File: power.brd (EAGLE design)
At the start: 186 x 186 mm, 126 parts, among them CN2 2X10 HEADER, Q1 IXTK180N15P, Q2 IXTK180N15P, Q3 2N7002, Q4 SPD15P10PL, Q5 2N7002, U1 LT1630, U10 LM2936, U11 LM317, U2 LT1630, U3 DCDC 15V, U4 DAC80501, U5 DAC80501, U6 ADS1120, U7 LM2662, U8 LM7805, U9 TPS3700

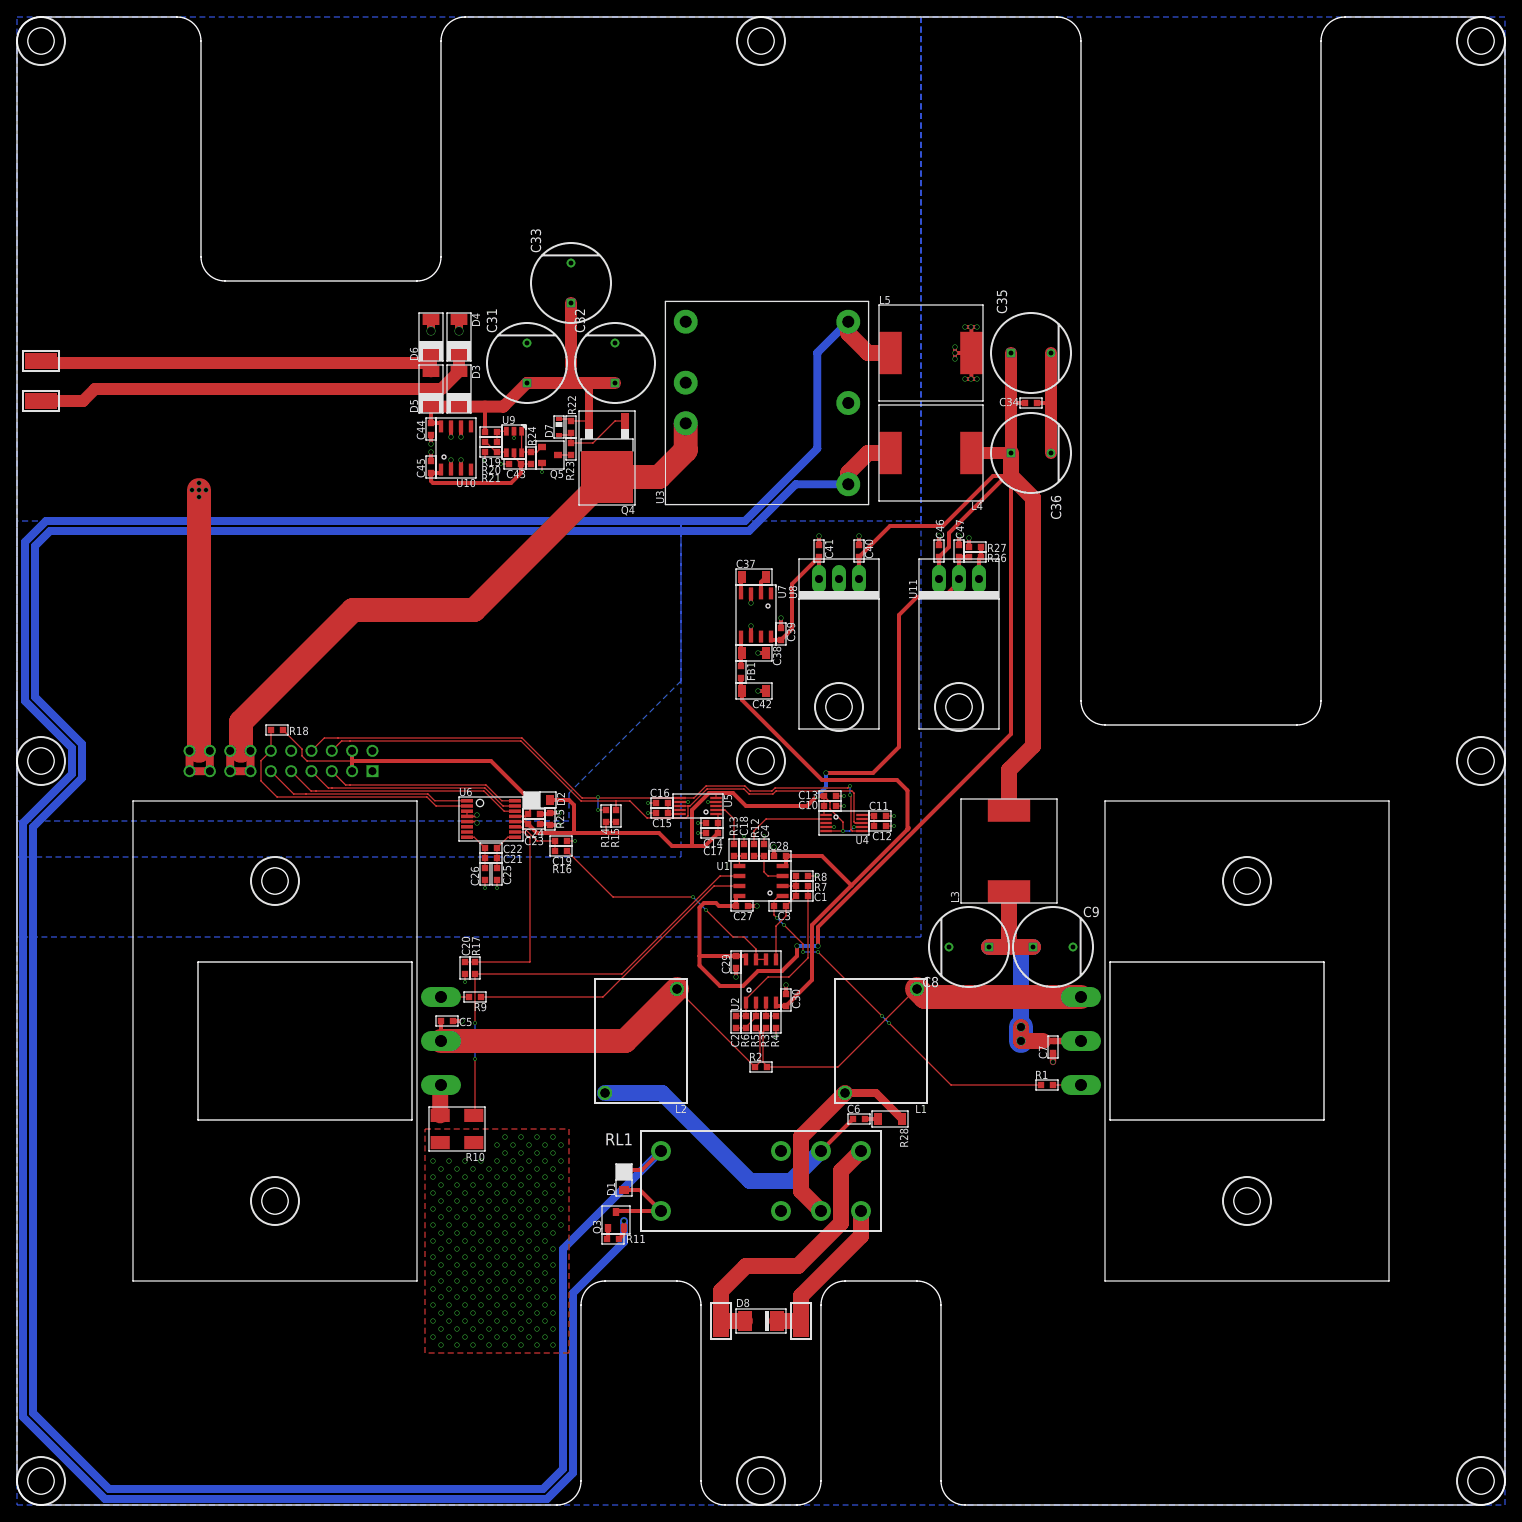
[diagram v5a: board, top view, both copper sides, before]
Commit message: DRC passes on both PCBs, pushed to Fusion
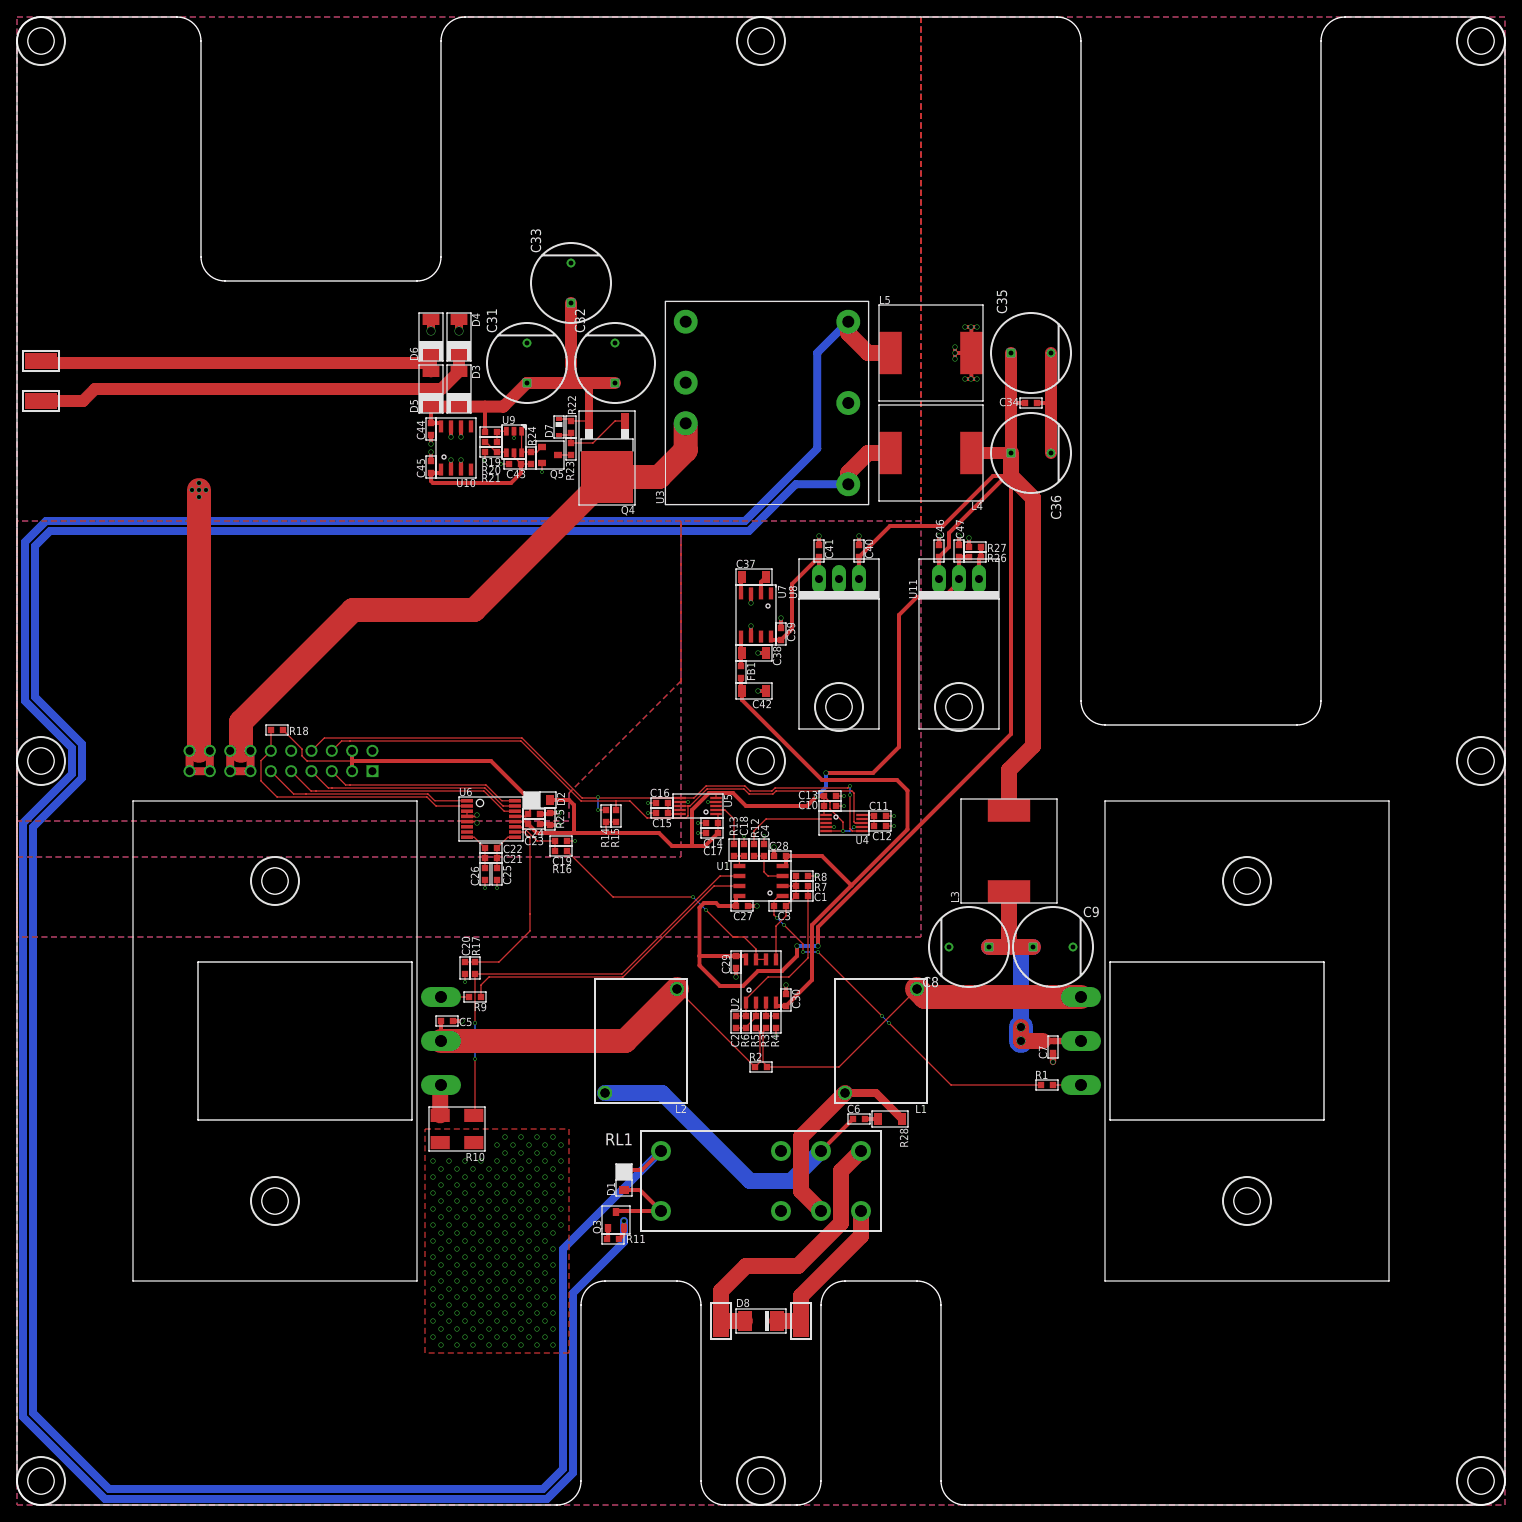
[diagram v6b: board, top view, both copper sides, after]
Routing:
- net ADC1_IOUT_SENSE: track 25.8 -> 23.5 mm
- net N$3: track 49.0 -> 50.4 mm
- net N$9: track 38.0 -> 38.9 mm
- added copper zone on layer 1, net DGND
- added copper zone on layer 1, net PGND
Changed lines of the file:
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@@
 <setting verticaltext="up"/>
 </settings>
-<grid distance="0.25" unitdist="mm" unit="mm" style="lines" multiple="1" display="yes" altdistance="0.125" altunitdist="mm" altunit="mm"/>
+<grid distance="0.125" unitdist="mm" unit="mm" style="lines" multiple="1" display="yes" altdistance="0.125" altunitdist="mm" altunit="mm"/>
 <layers>
 <layer number="1" name="Top" color="4" fill="1" visible="yes" active="yes"/>
@@
 </layers>
 <board>
-<fusionsync huburn="a.cGVyc29uYWw6dWUyYjllNWFm" projecturn="a.cGVyc29uYWw6dWUyYjllNWFmIzIwMjAwODI1MzI2NDUzNDMx" f3durn="urn:adsk.wipprod:dm.lineage:_9x5qJVdRZCpXJjkiumNtQ" pcbguid="" lastpulledtime="" lastsyncedchangeguid="" latestrevisionid="937367c5-8238-4ad7-90b2-8c012174326e" lastsyncedrevisionid="937367c5-8238-4ad7-90b2-8c012174326e" lastboardhashguid="3eac3db8-99fa-0ddd-d299-2097d3309fd4" lastpushedtime="2020-10-07T18:52:01Z" linktopcb3d="true"/>
+<fusionsync huburn="a.cGVyc29uYWw6dWUyYjllNWFm" projecturn="a.cGVyc29uYWw6dWUyYjllNWFmIzIwMjAwODI1MzI2NDUzNDMx" f3durn="urn:adsk.wipprod:dm.lineage:_9x5qJVdRZCpXJjkiumNtQ" pcbguid="" lastpulledtime="" lastsyncedchangeguid="" latestrevisionid="8ecf1d17-d364-4a8b-8f83-d8dd12726b38" lastsyncedrevisionid="8ecf1d17-d364-4a8b-8f83-d8dd12726b38" lastboardhashguid="6223c045-1d6c-c285-163c-80cf67557d4e" lastpushedtime="2020-10-08T18:05:57Z" linktopcb3d="true"/>
 <plain>
 <wire x1="90" y1="-93" x2="93" y2="-90" width="0" layer="20" curve="90" locked="yes"/>
@@
 <wire x1="0.625" y1="-33.5" x2="0.25" y2="-33.875" width="0.15" layer="1"/>
 <wire x1="0.75" y1="-38.125" x2="0.75" y2="-38.25" width="0.15" layer="1"/>
-<wire x1="0.75" y1="-38.25" x2="9.625" y2="-38.25" width="0.15" layer="1"/>
-<wire x1="19.5" y1="-28.375" x2="9.625" y2="-38.25" width="0.15" layer="1"/>
+<wire x1="0.75" y1="-38.25" x2="9.75" y2="-38.25" width="0.15" layer="1"/>
+<wire x1="18.625" y1="-29.375" x2="9.75" y2="-38.25" width="0.15" layer="1"/>
 <wire x1="20.5" y1="-29.5" x2="19.5" y2="-28.5" width="3" layer="1"/>
 <wire x1="0.25" y1="-33.875" x2="0.25" y2="-37.625" width="0.15" layer="1"/>
 <wire x1="0.25" y1="-37.625" x2="0.75" y2="-38.125" width="0.15" layer="1"/>
-<wire x1="19.5" y1="-28.5" x2="19.5" y2="-28.375" width="0" layer="19" extent="1-1"/>
+<wire x1="19.5" y1="-28.5" x2="20.5" y2="-29.5" width="0.15" layer="1"/>
+<wire x1="19.5" y1="-28.5" x2="18.625" y2="-29.375" width="0.15" layer="1"/>
 </signal>
 <signal name="N$4">
@@
 <wire x1="-35.675" y1="-7.575" x2="-35.5" y2="-7.75" width="0.25" layer="1"/>
 <via x="-35.5" y="-7.75" extent="1-16" drill="0.5"/>
+<polygon width="0.15" layer="1" rank="2">
+<vertex x="-93" y="-93"/>
+<vertex x="93" y="-93"/>
+<vertex x="93" y="93"/>
+<vertex x="20" y="93"/>
+<vertex x="20" y="30"/>
+<vertex x="-10" y="30"/>
+<vertex x="-10" y="10"/>
+<vertex x="-24" y="-4"/>
+<vertex x="-24" y="-7.5"/>
+<vertex x="-93" y="-7.5"/>
+</polygon>
 </signal>
 <signal name="N$10">
@@
 <contactref element="R9" pad="1"/>
 <contactref element="U1" pad="7"/>
-<wire x1="-35" y1="-29.5" x2="-19.75" y2="-29.5" width="0.15" layer="1"/>
+<wire x1="-35" y1="-29.5" x2="-35" y2="-28" width="0.15" layer="1"/>
+<wire x1="-34" y1="-27" x2="-35" y2="-28" width="0.15" layer="1"/>
+<wire x1="-17.25" y1="-27" x2="-34" y2="-27" width="0.15" layer="1"/>
 <wire x1="-5.875" y1="-15.625" x2="-2.7" y2="-15.625" width="0.15" layer="1"/>
-<wire x1="-19.75" y1="-29.5" x2="-5.875" y2="-15.625" width="0.15" layer="1"/>
+<wire x1="-17.25" y1="-27" x2="-5.875" y2="-15.625" width="0.15" layer="1"/>
 </signal>
 <signal name="N$11">
@@
 <wire x1="-30.75" y1="-8.875" x2="-29.625" y2="-8.875" width="0.15" layer="1"/>
 <wire x1="-29.625" y1="-8.875" x2="-28.875" y2="-9.625" width="0.15" layer="1"/>
-<wire x1="-35.75" y1="-25.125" x2="-28.875" y2="-25.125" width="0.15" layer="1"/>
-<wire x1="-28.875" y1="-25.125" x2="-28.875" y2="-9.625" width="0.15" layer="1"/>
+<wire x1="-35.75" y1="-25.125" x2="-32.75" y2="-25.125" width="0.15" layer="1"/>
+<wire x1="-28.875" y1="-19.125" x2="-28.875" y2="-9.625" width="0.15" layer="1"/>
+<wire x1="-32.75" y1="-25.125" x2="-28.875" y2="-21.25" width="0.1524" layer="1"/>
+<wire x1="-28.875" y1="-21.25" x2="-28.875" y2="-19.125" width="0.1524" layer="1"/>
 </signal>
 <signal name="N$12">
@@
 <wire x1="10.875" y1="-3.375" x2="1.75" y2="-3.375" width="0.15" layer="1"/>
 <wire x1="12.625" y1="-8.75" x2="11.375" y2="-8.75" width="0.15" layer="1"/>
-<wire x1="11.25" y1="-4.375" x2="11.125" y2="-4.25" width="0.15" layer="1"/>
 <via x="11.125" y="-4.25" extent="1-16" drill="0.3"/>
 <wire x1="11.125" y1="-4.25" x2="11.125" y2="-3.125" width="0.15" layer="16"/>
 <via x="11.125" y="-3.125" extent="1-16" drill="0.3"/>
 <wire x1="11.125" y1="-3.125" x2="10.875" y2="-3.375" width="0.15" layer="1"/>
-<wire x1="11.375" y1="-8.75" x2="11.25" y2="-8.625" width="0.15" layer="1"/>
-<wire x1="11.25" y1="-8.625" x2="11.25" y2="-4.375" width="0.15" layer="1"/>
+<wire x1="11.375" y1="-8.75" x2="11.125" y2="-8.5" width="0.15" layer="1"/>
+<wire x1="11.125" y1="-8.5" x2="11.125" y2="-4.25" width="0.15" layer="1"/>
 <wire x1="1.75" y1="-3.375" x2="1.375" y2="-3.75" width="0.15" layer="1"/>
 <wire x1="-6.875" y1="-3.125" x2="-8.375" y2="-4.625" width="0.15" layer="1"/>
@@
 <wire x1="-20.375" y1="-4.5" x2="-20.375" y2="-4.625" width="0.15" layer="1"/>
 <wire x1="-22.375" y1="-4.625" x2="-29.875" y2="2.875" width="0.15" layer="1"/>
-<wire x1="-29.875" y1="2.875" x2="-52.875" y2="2.875" width="0.15" layer="1"/>
+<wire x1="-29.875" y1="2.875" x2="-54.585" y2="2.875" width="0.15" layer="1"/>
 <contactref element="CN2" pad="17"/>
-<wire x1="-52.875" y1="2.875" x2="-54.585" y2="2.875" width="0.15" layer="1"/>
 <wire x1="-54.585" y1="2.875" x2="-56.19" y2="1.27" width="0.15" layer="1"/>
 </signal>
@@
 <contactref element="CN2" pad="20"/>
 <contactref element="CN2" pad="16"/>
+<polygon width="0.15" layer="1" rank="4">
+<vertex x="-10" y="30"/>
+<vertex x="-93" y="30"/>
+<vertex x="-93" y="-12"/>
+<vertex x="-10" y="-12"/>
+</polygon>
 </signal>
 <signal name="N$345">
@@
 <wire x1="-5.125" y1="-14.375" x2="-17.375" y2="-26.625" width="0.15" layer="1"/>
 <via x="-35.75" y="-32.75" extent="1-16" drill="0.35"/>
-<wire x1="-35.9" y1="-44.3" x2="-35.85" y2="-44.25" width="0.15" layer="1"/>
 <wire x1="-17.375" y1="-26.625" x2="-35.75" y2="-26.625" width="0.15" layer="1"/>
 <wire x1="-35.75" y1="-26.625" x2="-35.75" y2="-32.75" width="0.15" layer="1"/>
 <wire x1="-35.75" y1="-32.75" x2="-35.75" y2="-37.25" width="0.15" layer="16"/>
 <via x="-35.75" y="-37.25" extent="1-16" drill="0.3"/>
+<wire x1="-35.75" y1="-44.15" x2="-35.75" y2="-37.25" width="0.15" layer="1"/>
 <wire x1="-35.9" y1="-44.3" x2="-35.75" y2="-44.15" width="0.15" layer="1"/>
-<wire x1="-35.75" y1="-37.25" x2="-35.75" y2="-44.15" width="0.15" layer="1"/>
 </signal>
 <signal name="3V3D">
@@
 <wire x1="6.375" y1="-20.5" x2="11.3125" y2="-15.5625" width="0.5" layer="1"/>
 <wire x1="11.3125" y1="-15.5625" x2="18.3125" y2="-8.5625" width="0.5" layer="1"/>
-<wire x1="18.3125" y1="-8.5625" x2="18.5" y2="-8.375" width="0.5" layer="1"/>
 <wire x1="3.125" y1="-11.875" x2="7.625" y2="-11.875" width="0.5" layer="1"/>
 <wire x1="7.625" y1="-11.875" x2="11.3125" y2="-15.5625" width="0.5" layer="1"/>
@@
 <wire x1="-70.25" y1="33.875" x2="-71.125" y2="33.875" width="0.5" layer="1"/>
 <via x="-71.125" y="33.875" extent="1-16" drill="0.5"/>
+<polygon width="0.15" layer="1" rank="6">
+<vertex x="-93" y="93"/>
+<vertex x="20" y="93"/>
+<vertex x="20" y="30"/>
+<vertex x="20" y="-22"/>
+<vertex x="-93" y="-22"/>
+</polygon>
 </signal>
 <signal name="N$37">

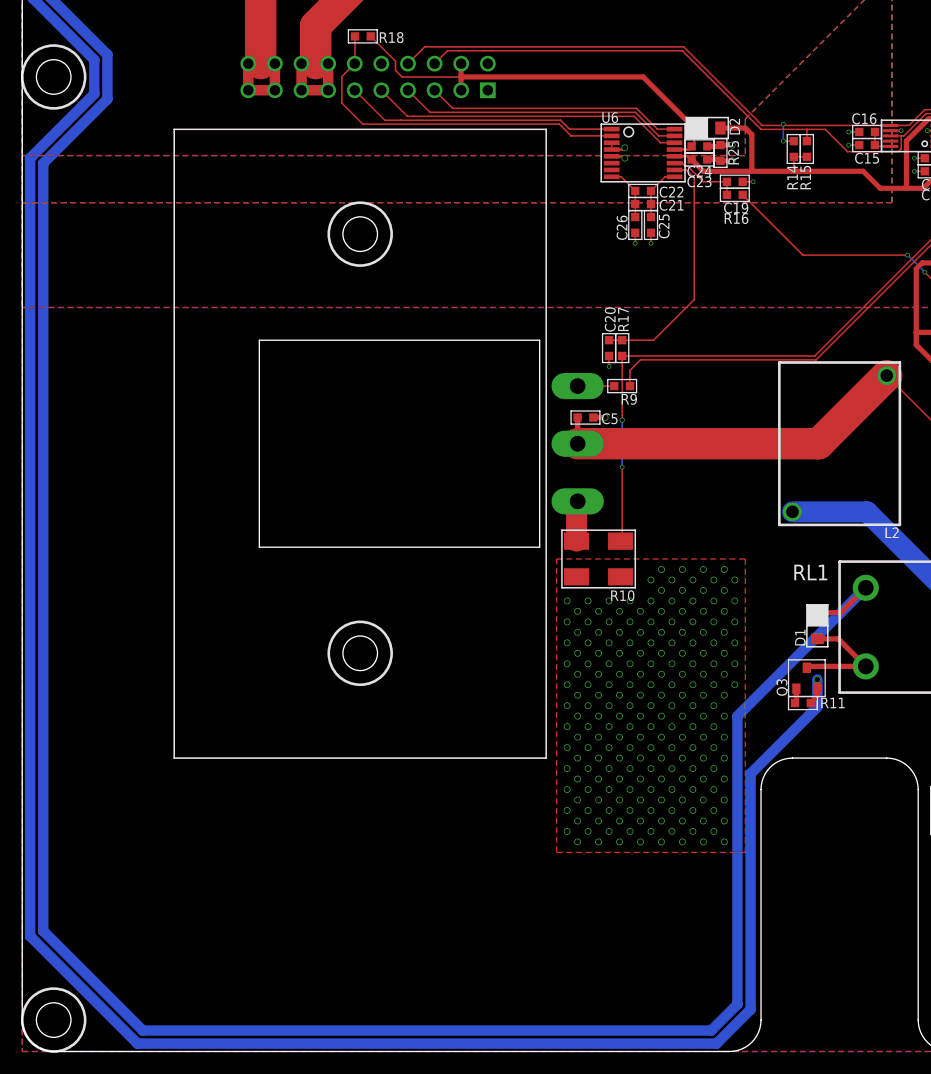
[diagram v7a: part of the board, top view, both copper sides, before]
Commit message: Added control for the output relay
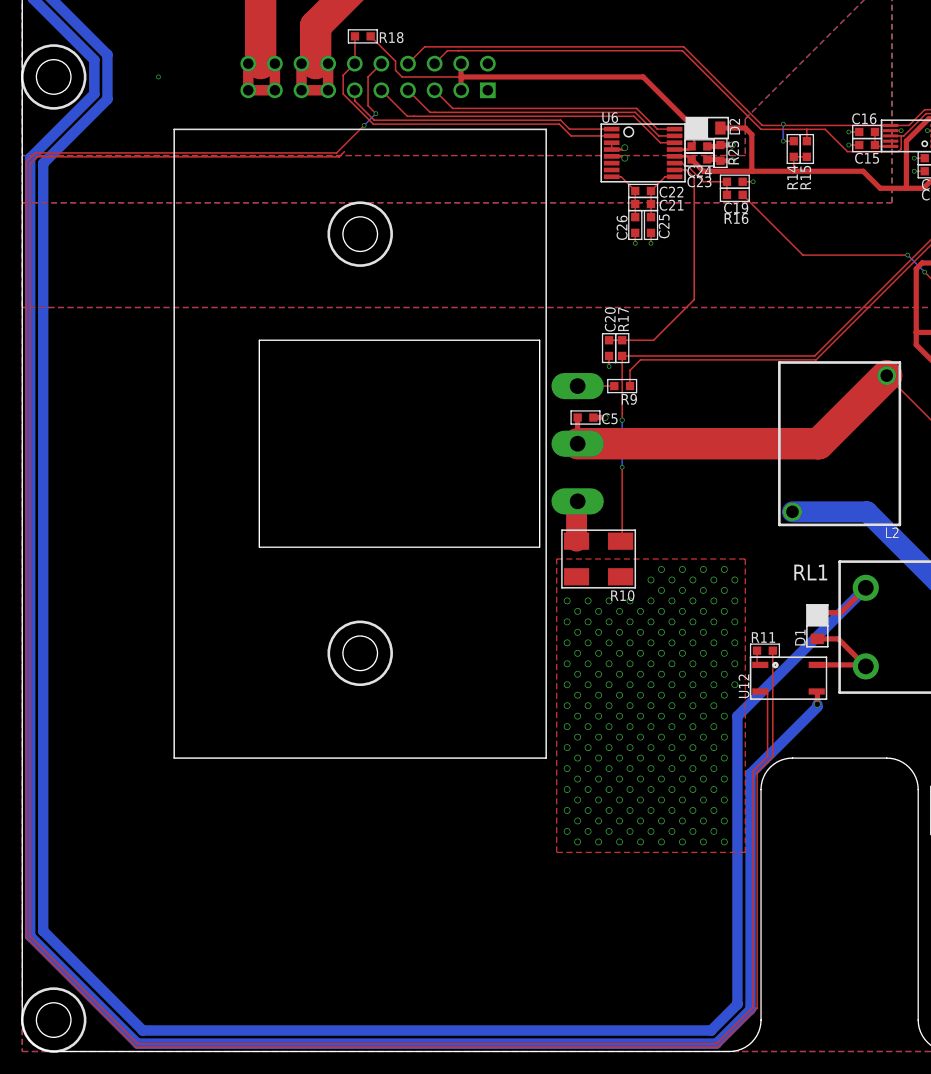
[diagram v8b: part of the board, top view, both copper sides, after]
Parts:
- removed Q3: 2N7002, TRANSISTORs:SOT23-3
- added U12: SPST SSR, ICs:CPC1002N
- R11: value 10k -> 820R
- moved R11 6.18 mm to (-22.1, -54.8)
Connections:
- new net N$13: R11.2, U12.1
- net DGND: now also U12.2; no longer CN2.16
- net GND: now also U12.3; no longer Q3.3, R11.1
- net N$19: now also U12.4; no longer Q3.2
- net OUTPUT_RLY_EN: now also CN2.16, R11.1; no longer Q3.1, R11.2
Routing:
- net OUTPUT_RLY_EN: track 1.43 -> 225.3 mm, vias 0 -> 2
- net DGND: track 4.40 -> 214.5 mm, vias 2 -> 3
- net GND: track 354.4 -> 350.8 mm
- net N$13: track 0.00 -> 1.63 mm
- net N$19: track 11.4 -> 10.5 mm
- net ADC_SPI_!CS: track 33.9 -> 33.2 mm
- net ADC_SPI_SCLK: track 26.1 -> 26.6 mm
